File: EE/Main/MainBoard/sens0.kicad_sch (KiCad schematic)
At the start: 3 parts, among them J1 Conn_02x13_Odd_Even

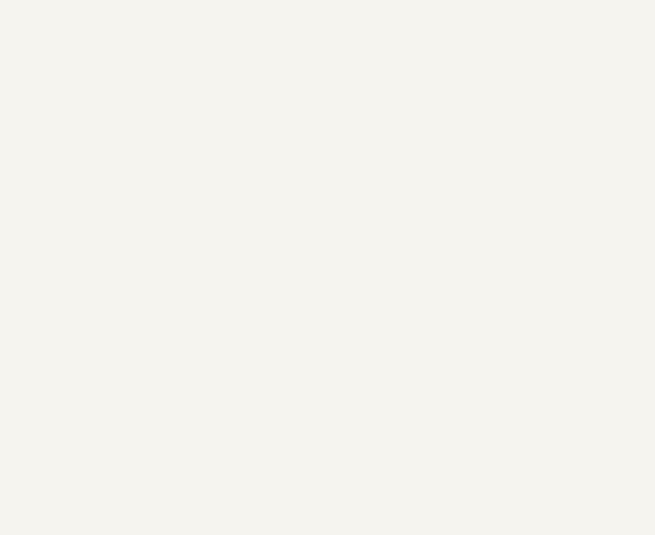
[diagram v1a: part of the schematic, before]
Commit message: WIP - Moving Sensor to IO Expander
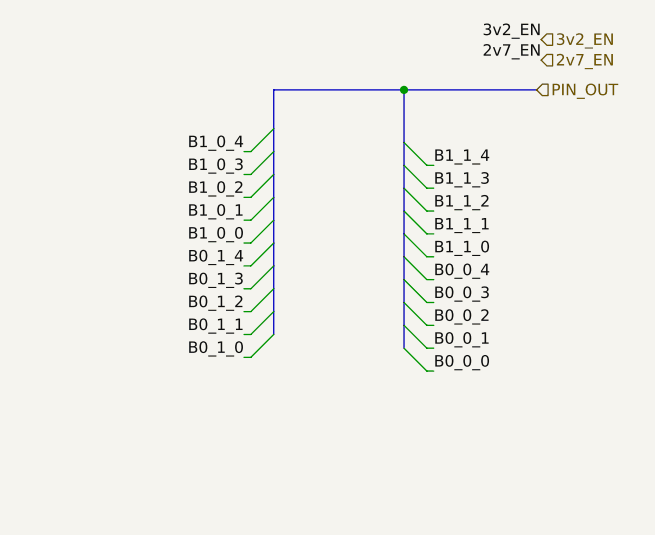
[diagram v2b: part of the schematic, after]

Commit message: Updated layout, and placement for main board
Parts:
- removed J1: Conn_02x13_Odd_Even, Connector_PinHeader_1.27mm:PinHeader_2x13_P1.27mm_Vertical_SMD, symbol Connector_Generic:Conn_02x13_Odd_Even
- added J1: Conn_01x04_Male, Connector_PinSocket_2.54mm:PinSocket_1x04_P2.54mm_Vertical, symbol Connector:Conn_01x04_Male
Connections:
- net GND: now also J1.4 (Pin_4)
- net VCC: now also J1.1 (Pin_1)
- new net SCL: J1.2 (Pin_2)
- new net SDA: J1.3 (Pin_3)
- no-connect marks 2 -> 0

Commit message: Routine Update
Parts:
- H1, H2: footprint MountingHole:MountingHole_2.5mm -> MountingHole:MountingHole_2.7mm
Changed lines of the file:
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@@
       (effects (font (size 1.27 1.27)) (justify left))
     )
-    (property "Footprint" "MountingHole:MountingHole_2.5mm" (id 2) (at 118.872 109.22 0)
+    (property "Footprint" "MountingHole:MountingHole_2.7mm" (id 2) (at 118.872 109.22 0)
       (effects (font (size 1.27 1.27)) hide)
     )
@@
       (effects (font (size 1.27 1.27)) (justify left))
     )
-    (property "Footprint" "MountingHole:MountingHole_2.5mm" (id 2) (at 118.872 65.024 0)
+    (property "Footprint" "MountingHole:MountingHole_2.7mm" (id 2) (at 118.872 65.024 0)
       (effects (font (size 1.27 1.27)) hide)
     )
